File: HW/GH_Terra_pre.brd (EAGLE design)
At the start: 160 x 100 mm, 59 parts, among them Q1 IRLML5203TRPBF, Q2 IRLML2030TRPBF, Q3 16MHz, Q4 IRLML5203TRPBF, Q5 IRLML2030TRPBF, Q6 BC817-40.215, Q7 BC817-40.215, U1 STM8L152C6T6

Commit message: REV1
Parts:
- removed C10: CC0603JRX7R9BB104, rcl:C0603_IPC
- removed C6, C8, C9: CC0603GRNPO9BN220, rcl:C0603_IPC
- removed L1: BLM18AG102SN1D, rcl:R0603_IPC
- removed PAD1, PAD2: (no value), wirepad:2,54/1,0
- removed Q3: 16MHz, crystal:HC49/S
- removed Q6, Q7: BC817-40.215, semicon-smd-ipc:SOT23
- removed R1: RC0603JR-0710RL, rcl:R0603_IPC
- removed R14, R18: RC0603JR-079R1L, rcl:R0603_IPC
- removed R15: CRCW06031K00JNEA, rcl:R0603_IPC
- removed R16, R19, R9: RC0603FR-07100KL, rcl:R0603_IPC
- removed R20, R21, R22, R23, R24, R25, R26: CR0603-FX-1002ELF, rcl:R0603_IPC
- removed SV2: (no value), con-lstb:MA03-1
- U$5: value (none) -> MA02-1; device rubber_key:RK_3X4 -> con-lstb:MA02-1
- moved U$5 41.2 mm to (110.0, 47.9), turned to 270 degrees
- moved SV1 17.0 mm to (69.8, 55.9)
- moved U$4 15.0 mm to (62.5, 38.2)
- moved C2 11.4 mm to (73.7, 49.6), turned to 270 degrees
- moved U$3 7.60 mm to (77.5, 38.2)
- moved U$2 7.30 mm to (99.7, 38.2)
- moved R4 6.41 mm to (98.7, 62.6), turned to 180 degrees
- moved R2 5.04 mm to (97.8, 59.2), turned to 90 degrees
- moved R12 4.07 mm to (100.0, 47.2)
- moved R11 3.99 mm to (100.0, 49.0)
- moved R10 3.70 mm to (97.3, 48.1)
- moved R13 3.60 mm to (102.9, 48.1)
- moved D1 3.54 mm to (105.5, 45.0)
- moved D2 3.51 mm to (105.5, 51.2)
- moved R3 3.05 mm to (92.9, 58.4)
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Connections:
- removed net N$1: Q1.2, Q4.2, R1.2
- removed net N$33: C8.1, R9.1, U$5.P$1, U1.45
- removed net N$35: Q6.1, Q7.3, R15.2
- removed net N$4: Q2.2, Q5.2, Q6.3, R4.1, R5.2
- removed net N$6: Q6.2, Q7.1, R14.1, R18.1
- removed net USART_RX: R16.1, SV2.2, U1.41
- removed net USART_TX: SV2.1, U1.42
- removed net VREF-: R24.2, R25.2, R26.1, U1.9
- removed net VREF2: C2.1, L1.1, R19.1, R23.1, U1.11
- removed net XTAL_IN: C6.1, Q3.2, U1.3
- removed net XTAL_OUT: C9.1, Q3.1, U1.4
- net GND: now also Q2.2, Q5.2, R4.1, R5.2, U1.9; no longer C6.2, C8.2, C9.2, Q7.2, R14.2, R18.2, R26.2, SV2.3, U$5.P$2
- net MCC: no longer R15.1
- net N$2: no longer C10.1
- net N$27: now also U$5.1; no longer PAD2.1
- net N$3: no longer C10.2
- net VCC: now also C2.1, Q1.2, Q4.2, U1.11; no longer L1.2, R1.1, R16.2, R22.2, R9.2
- net VREF: no longer R19.2, R20.1, R24.1
- net VREF+: no longer R20.2, R21.1, R22.1, R23.2
- net VREF1: now also U$5.2; no longer PAD1.1, R21.2, R25.1
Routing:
- net VREF: track 82.0 -> 26.2 mm, vias 4 -> 2
- net VREF1: track 102.6 -> 48.9 mm, vias 3 -> 0
- net USART_RX: track 48.1 -> 0.00 mm, vias 2 -> 0
- net USART_TX: track 44.7 -> 0.00 mm, vias 1 -> 0
- net N$1: track 38.8 -> 0.00 mm, vias 3 -> 0
- net VREF+: track 35.1 -> 0.01 mm, vias 2 -> 0
- net VREF-: track 34.4 -> 0.00 mm, vias 2 -> 0
- net N$33: track 32.3 -> 0.00 mm, vias 1 -> 0
- net VREF2: track 27.3 -> 0.00 mm, vias 2 -> 0
- net N$4: track 21.5 -> 0.00 mm
- net VALVE_CLOSE: track 52.3 -> 31.0 mm
- net N$6: track 18.0 -> 0.00 mm
- net SWIM: track 31.7 -> 14.0 mm
- net RESET: track 37.3 -> 20.3 mm, vias 0 -> 1
- net N$35: track 16.0 -> 0.00 mm, vias 2 -> 0
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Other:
- outline, holes or cut-outs redrawn
- board text added: "GH_Terra_rev1"
- board text removed: "GH_Terra_rev0"
- board text removed: "vref+_most"
- board text removed: "vref+_most1"
- board text removed: "vref+_vcc"
- board text removed: "vref+_vdda"
- board text removed: "vref-_gnd"
- board text removed: "vref-_most"
- board text removed: "vref-_most1"

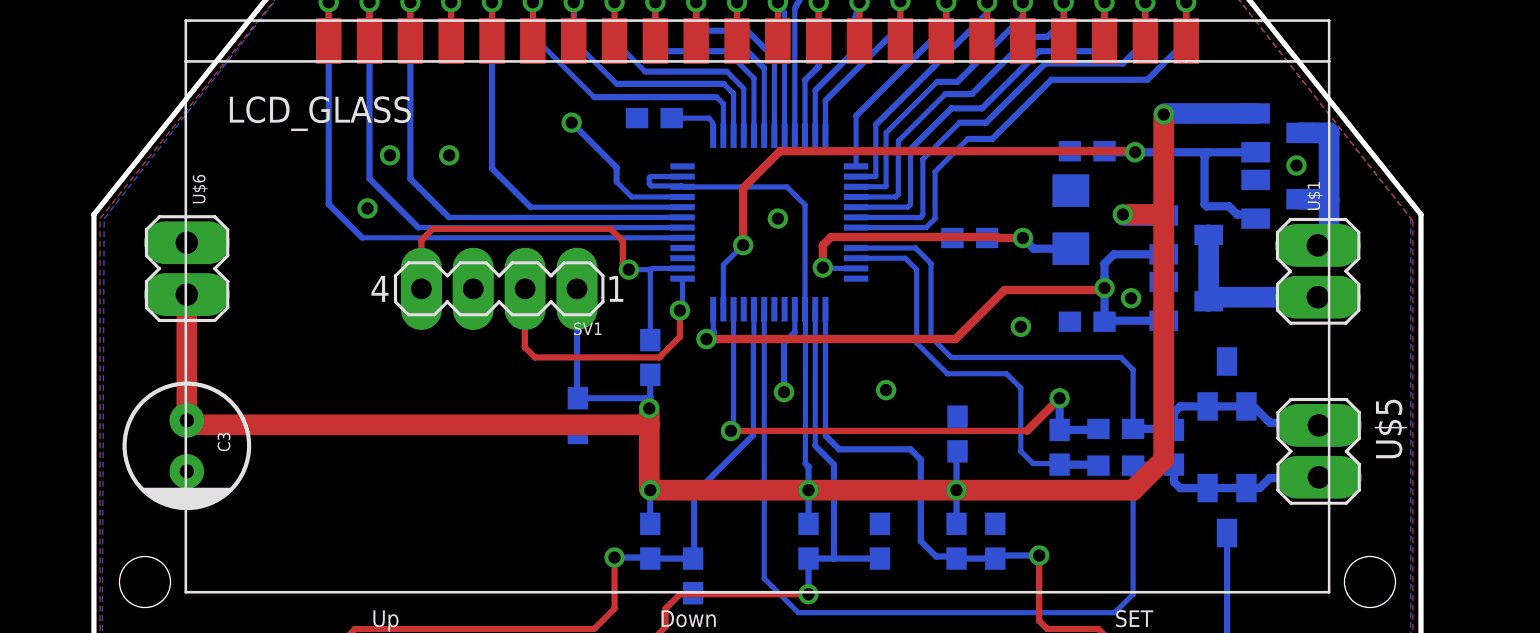
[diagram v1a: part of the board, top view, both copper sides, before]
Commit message: Закостылили мерцание показаний датчика влажности. Гореть мне в Аду за это....
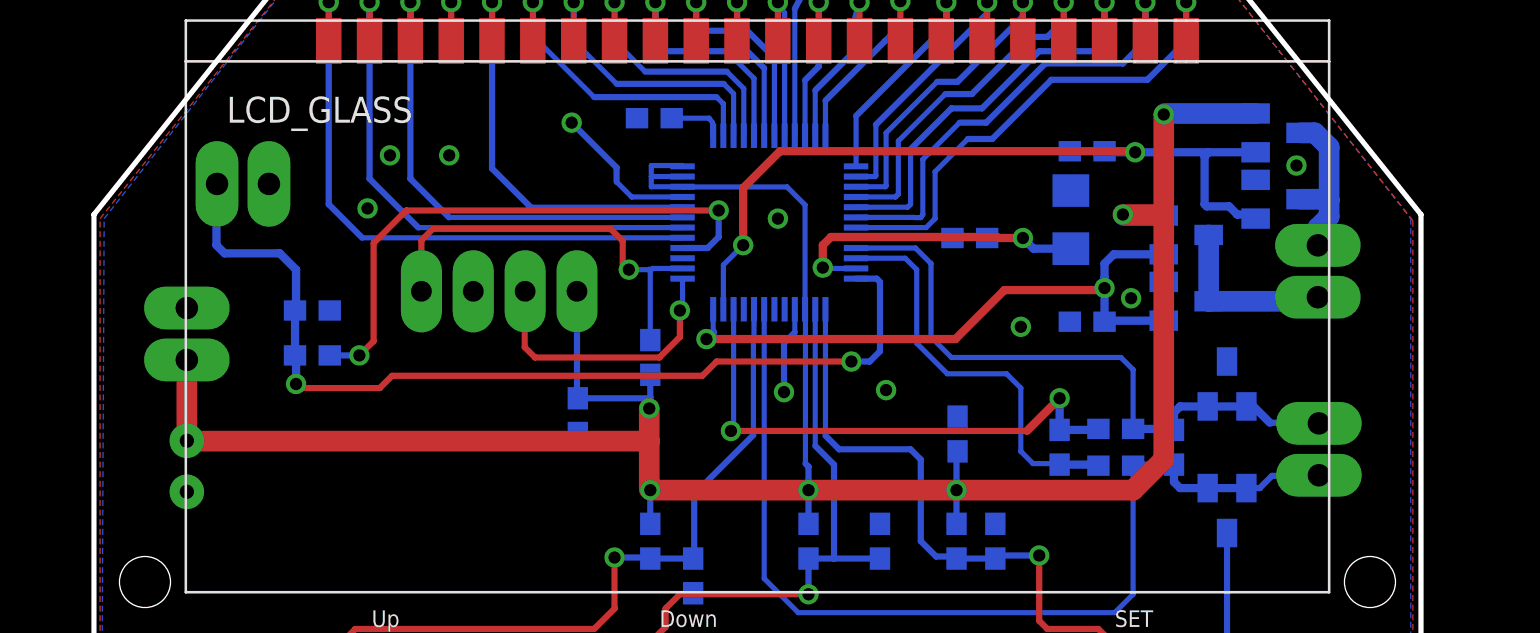
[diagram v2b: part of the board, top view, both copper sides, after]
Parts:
- added C6: CC0603JRX7R9BB104, rcl:C0603_IPC
- added R1: RC0603FR-07100KL, rcl:R0603_IPC
- added U7: MA02-1, con-lstb:MA02-1
- Q1, Q4: value IRLML5203TRPBF -> IRLML6402
- Q2, Q5: value IRLML2030TRPBF -> IRLML6244
- moved U$6 3.20 mm to (54.5, 53.6), flipped to the bottom
- moved C3 1.00 mm to (54.5, 47.2), flipped to the bottom
- moved SV1 0.12 mm to (69.8, 55.7), flipped to the bottom, turned to 0 degrees
- moved U$5 0.10 mm to (110.0, 48.0), flipped to the bottom
- flipped U$1 to the bottom
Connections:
- removed net MCC: U1.36
- removed net VREF+: U1.12
- new net CHECK_POS: R1.1, U1.4
- new net STATE: C6.1, R1.2, U1.36, U7.1
- net GND: now also C6.2, U7.2
- net VCC: now also U1.12
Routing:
- net STATE: track 0.00 -> 47.1 mm, vias 0 -> 2
- net CHECK_POS: track 0.00 -> 28.1 mm, vias 0 -> 2
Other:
- board text added: "SWIM"

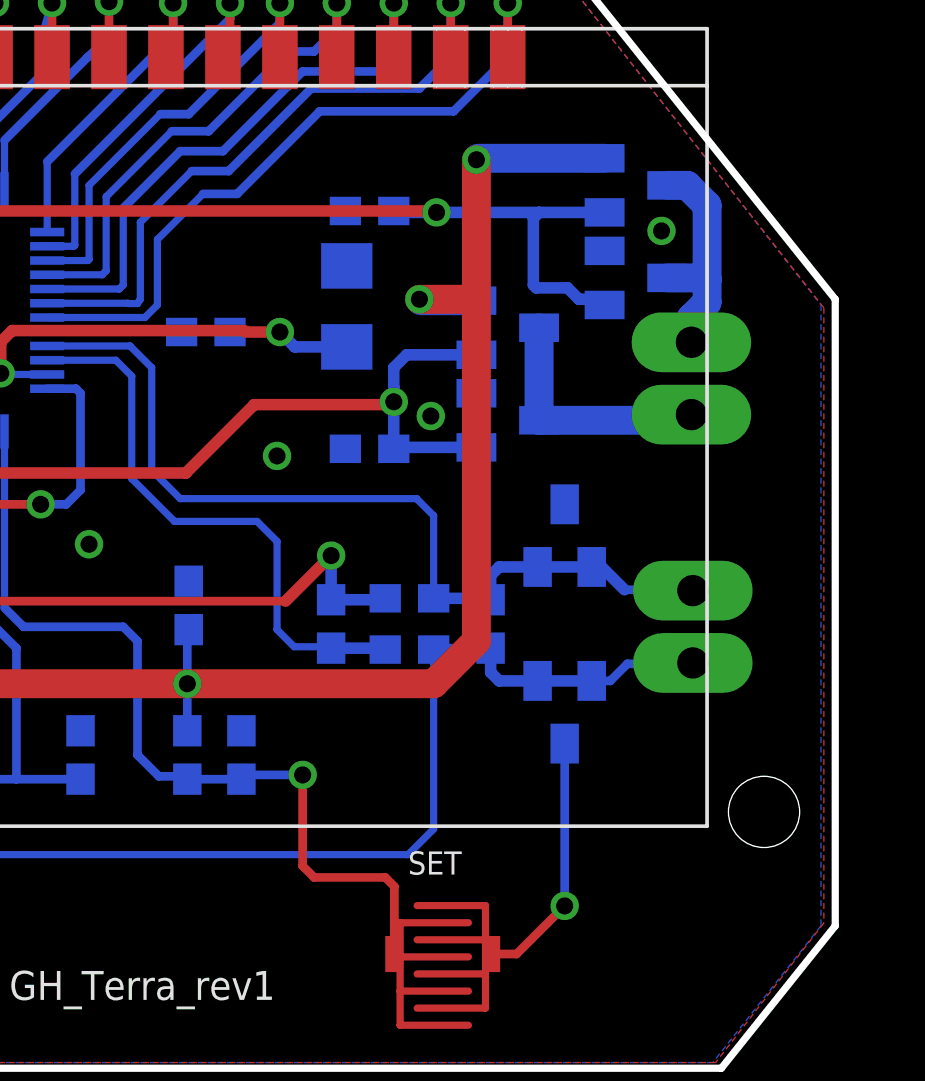
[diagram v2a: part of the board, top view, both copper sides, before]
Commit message: Введено: Защитный интервал между поливами. В сервисное меню добавлена настройка защитного интервала
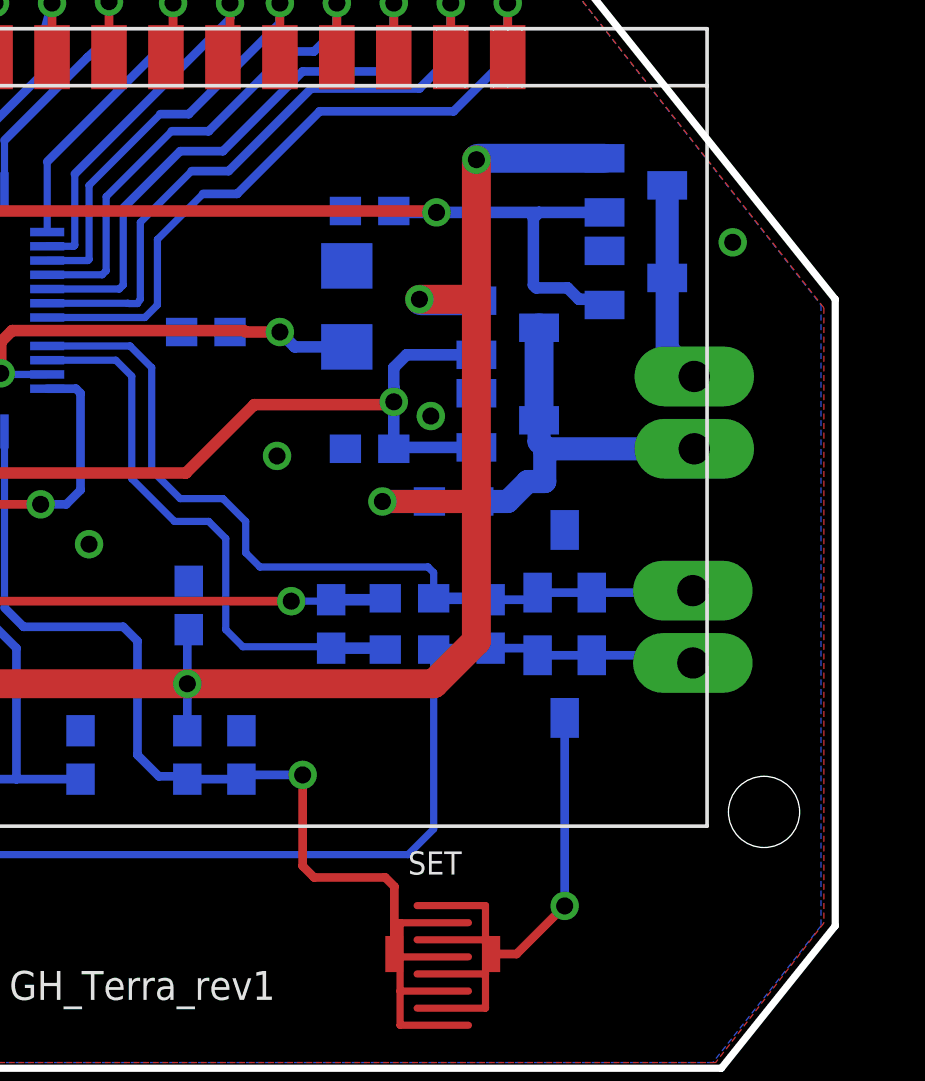
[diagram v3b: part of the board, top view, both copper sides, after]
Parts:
- added R9: RC0603FR-0727KL, rcl:R0603_IPC
- moved U$1 1.20 mm to (110.0, 55.5)
- moved D2 0.90 mm to (105.5, 50.3)
- moved D1 0.90 mm to (105.5, 45.9)
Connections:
- net N$3: now also R9.2
- net VCC: now also R9.1
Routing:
- net VCC: track 126.0 -> 131.0 mm, vias 6 -> 7
- net N$3: track 8.68 -> 13.4 mm
- net VREF: track 26.2 -> 24.1 mm
- net N$27: track 31.5 -> 29.8 mm
- net N$2: track 8.15 -> 7.10 mm
- net VREF1: track 49.0 -> 48.0 mm
- net GND: track 59.1 -> 60.0 mm

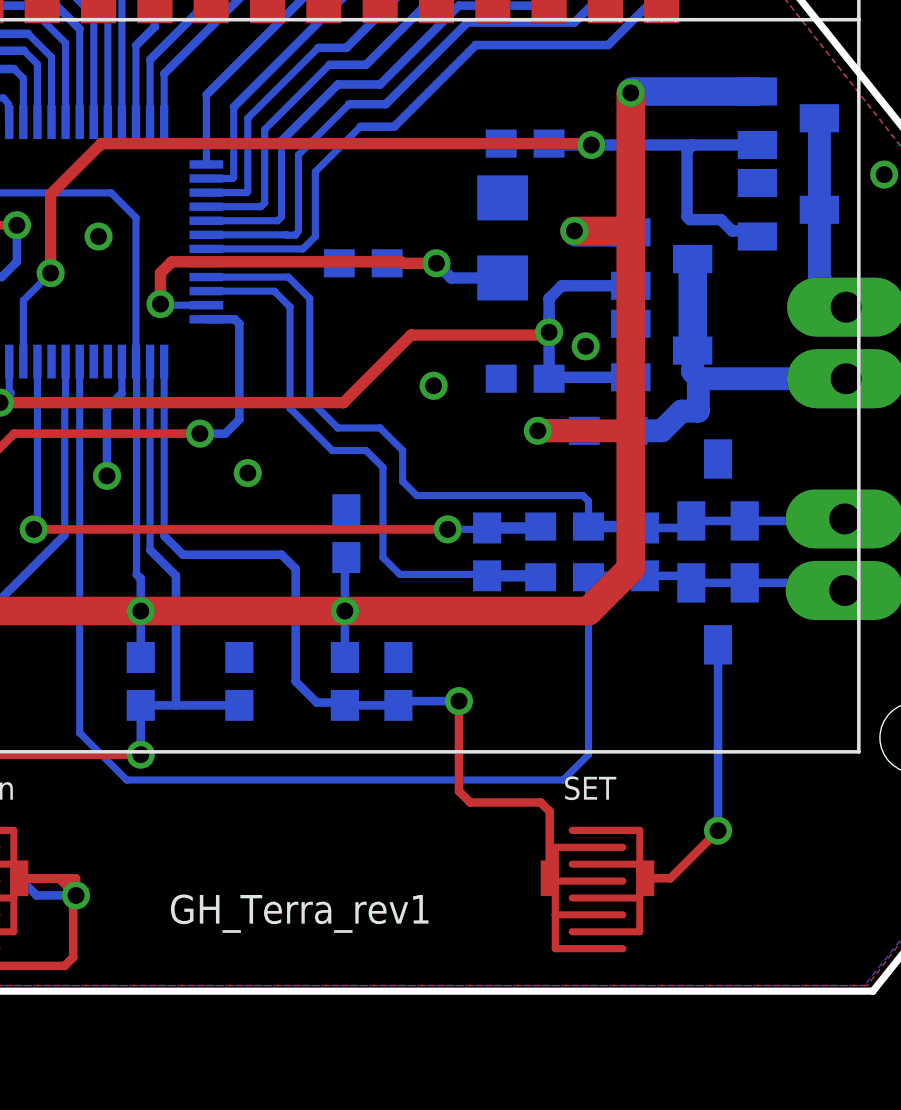
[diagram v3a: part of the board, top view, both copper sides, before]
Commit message: Версия для односторонней платой. Первая редакция. Перенастроены порты и проверены все основные функции
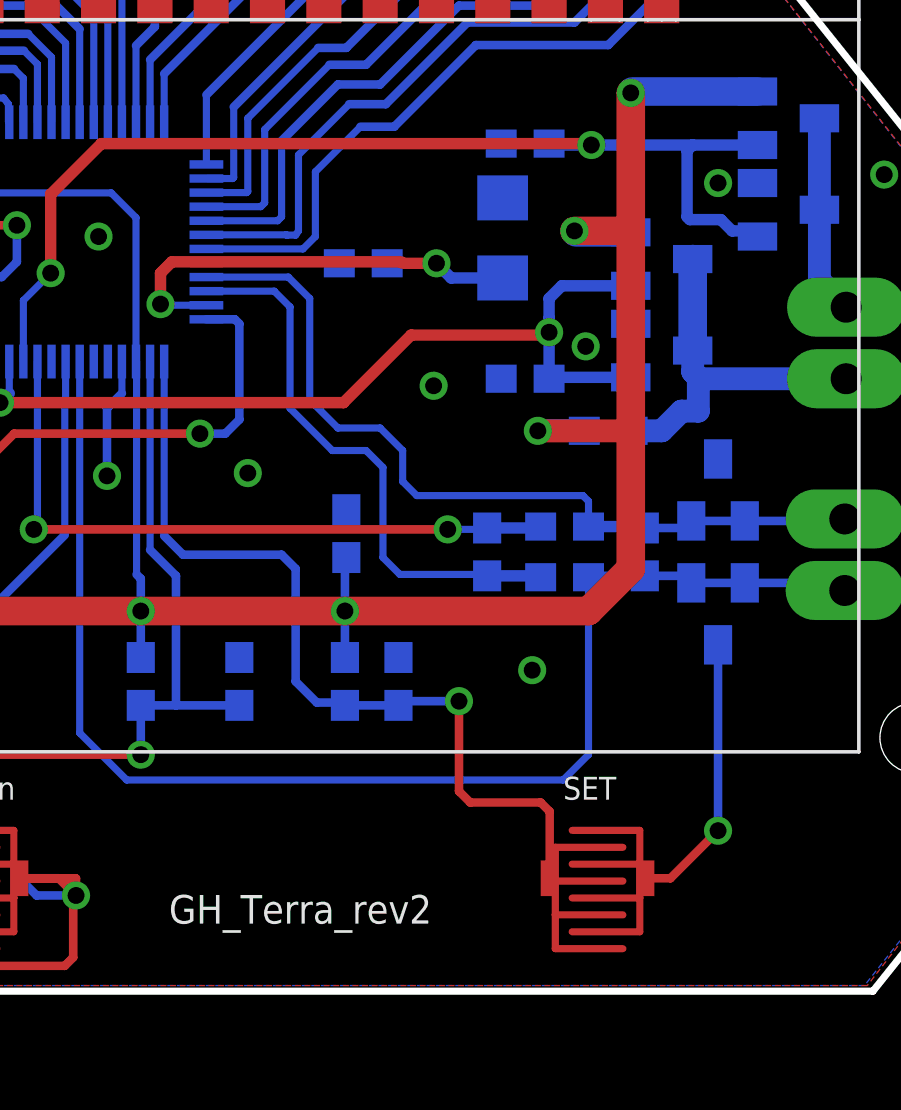
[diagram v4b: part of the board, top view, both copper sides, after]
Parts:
- R10, R11, R12, R13: value RC0603FR-0727KL -> 1k_1%
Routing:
- net GND: vias 16 -> 18
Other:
- board text added: "GH_Terra_rev2"
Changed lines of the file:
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@@
 <text x="77.7" y="39.3" size="0.8128" layer="25">Down</text>
 <text x="95.1" y="36.8" size="1.016" layer="22" rot="MR0">GH_Terra_rev1</text>
-<text x="86" y="34.9" size="1.016" layer="21">GH_Terra_rev1</text>
+<text x="86" y="34.9" size="1.016" layer="21">GH_Terra_rev2</text>
 <rectangle x1="62.3" y1="33.8" x2="65.7" y2="38.5" layer="100"/>
 <rectangle x1="77.3" y1="33.8" x2="80.7" y2="38.4" layer="100"/>
@@
 <attribute name="VALUE" x="81.23" y="56.27" size="1.27" layer="28" rot="MR90"/>
 </element>
-<element name="R10" library="rcl" package="R0603_IPC" value="RC0603FR-0727KL" x="97.3" y="48.1" smashed="yes" rot="MR270">
+<element name="R10" library="rcl" package="R0603_IPC" value="1k_1%" x="97.3" y="48.1" smashed="yes" rot="MR270">
 <attribute name="NAME" x="96.665" y="48.735" size="0.6096" layer="26" rot="MR270"/>
 <attribute name="VALUE" x="99.205" y="48.735" size="1.27" layer="28" rot="MR270"/>
 </element>
-<element name="R11" library="rcl" package="R0603_IPC" value="RC0603FR-0727KL" x="100.05" y="49" smashed="yes" rot="MR0">
+<element name="R11" library="rcl" package="R0603_IPC" value="1k_1%" x="100.05" y="49" smashed="yes" rot="MR0">
 <attribute name="NAME" x="100.685" y="49.635" size="0.6096" layer="26" rot="MR0"/>
 <attribute name="VALUE" x="100.685" y="47.095" size="1.27" layer="28" rot="MR0"/>
 </element>
-<element name="R12" library="rcl" package="R0603_IPC" value="RC0603FR-0727KL" x="100.05" y="47.2" smashed="yes" rot="MR0">
+<element name="R12" library="rcl" package="R0603_IPC" value="1k_1%" x="100.05" y="47.2" smashed="yes" rot="MR0">
 <attribute name="NAME" x="100.685" y="47.835" size="0.6096" layer="26" rot="MR0"/>
 <attribute name="VALUE" x="100.685" y="45.295" size="1.27" layer="28" rot="MR0"/>
 </element>
-<element name="R13" library="rcl" package="R0603_IPC" value="RC0603FR-0727KL" x="102.9" y="48.1" smashed="yes" rot="MR270">
+<element name="R13" library="rcl" package="R0603_IPC" value="1k_1%" x="102.9" y="48.1" smashed="yes" rot="MR270">
 <attribute name="NAME" x="102.265" y="48.735" size="0.6096" layer="26" rot="MR270"/>
 <attribute name="VALUE" x="104.805" y="48.735" size="1.27" layer="28" rot="MR270"/>
@@
 <contactref element="C6" pad="2"/>
 <contactref element="U7" pad="2"/>
+<via x="98.9" y="43.9" extent="1-16" drill="0.6"/>
+<via x="105.5" y="61.2" extent="1-16" drill="0.6"/>
 </signal>
 <signal name="VCC">
